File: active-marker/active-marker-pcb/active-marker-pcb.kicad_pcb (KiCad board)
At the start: 2 copper layers, 45 x 35 mm, 47 parts, among them J1 Conn_01x10, J13 Conn_01x04, J2 Conn_01x04, J3 Conn_01x04, J4 Conn_01x04, J5 Conn_01x04, J6 Conn_01x04, J7 Conn_01x04, SW1 SW_DIP_x02, SW2 SW_Push, SW3 SW_Push, SW4 SW_Push, U1 220ADA16, U2 XC6206PxxxMR, U3 VEML6030, U4 VEML6030, U5 MCP2551-I-P, U6 STM32F303K8Tx, Y1 NX3225GA-32M

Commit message: add diode, fix gerber files
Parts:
- added D3: D_Schottky, Diode_SMD:D_SOD-523, B.Cu at (107.2, 99.8)
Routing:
- net +5V: track 88.7 -> 90.9 mm
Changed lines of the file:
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@@
+    )
+  )
+  (footprint "Diode_SMD:D_SOD-523" (layer "B.Cu")
+    (at 107.188 99.786 -90)
+    (descr "http://www.diodes.com/datasheets/ap02001.pdf p.144")
+    (tags "Diode SOD523")
+    (property "Sheetfile" "active-marker-pcb.kicad_sch")
+    (property "Sheetname" "")
+    (attr smd)
+    (fp_text reference "D3" (at 2.322 0 90) (layer "B.SilkS")
+      (effects (font (size 1 1) (thickness 0.15)) (justify mirror))
+    )
+    (fp_text value "D_Schottky" (at 0 -1.4 90) (layer "B.Fab")
+      (effects (font (size 1 1) (thickness 0.15)) (justify mirror))
+    )
+    (fp_text user "${REFERENCE}" (at 0 1.3 90) (layer "B.Fab")
+      (effects (font (size 1 1) (thickness 0.15)) (justify mirror))
+    )
+    (fp_line (start 0.7 -0.6) (end -1.15 -0.6) (layer "B.SilkS") (width 0.12))
+    (fp_line (start -1.15 0.6) (end -1.15 -0.6) (layer "B.SilkS") (width 0.12))
+    (fp_line (start 0.7 0.6) (end -1.15 0.6) (layer "B.SilkS") (width 0.12))
+    (fp_line (start -1.25 -0.7) (end -1.25 0.7) (layer "B.CrtYd") (width 0.05))
+    (fp_line (start -1.25 0.7) (end 1.25 0.7) (layer "B.CrtYd") (width 0.05))
+    (fp_line (start 1.25 -0.7) (end -1.25 -0.7) (layer "B.CrtYd") (width 0.05))
+    (fp_line (start 1.25 0.7) (end 1.25 -0.7) (layer "B.CrtYd") (width 0.05))
+    (fp_line (start -0.2 -0.2) (end -0.2 0.2) (layer "B.Fab") (width 0.1))
+    (fp_line (start 0.1 0) (end 0.25 0) (layer "B.Fab") (width 0.1))
+    (fp_line (start -0.2 0) (end -0.35 0) (layer "B.Fab") (width 0.1))
+    (fp_line (start -0.65 0.45) (end 0.65 0.45) (layer "B.Fab") (width 0.1))
+    (fp_line (start -0.2 0) (end 0.1 -0.2) (layer "B.Fab") (width 0.1))
+    (fp_line (start 0.65 -0.45) (end -0.65 -0.45) (layer "B.Fab") (width 0.1))
+    (fp_line (start 0.65 0.45) (end 0.65 -0.45) (layer "B.Fab") (width 0.1))
+    (fp_line (start 0.1 0.2) (end -0.2 0) (layer "B.Fab") (width 0.1))
+    (fp_line (start -0.65 -0.45) (end -0.65 0.45) (layer "B.Fab") (width 0.1))
+    (fp_line (start 0.1 -0.2) (end 0.1 0.2) (layer "B.Fab") (width 0.1))
+    (pad "1" smd rect (at -0.7 0 90) (size 0.6 0.7) (layers "B.Cu" "B.Paste" "B.Mask")
+      (net 1 "+5V") (pinfunction "K") (pintype "passive"))
+    (pad "2" smd rect (at 0.7 0 90) (size 0.6 0.7) (layers "B.Cu" "B.Paste" "B.Mask")
+      (net 3 "+3V3") (pinfunction "A") (pintype "passive"))
+    (model "${KICAD6_3DMODEL_DIR}/Diode_SMD.3dshapes/D_SOD-523.wrl"
+      (offset (xyz 0 0 0))
+      (scale (xyz 1 1 1))
+      (rotate (xyz 0 0 0))
     )
   )
@@
   (segment (start 118.074 115.606) (end 118.074 114.707) (width 0.3) (layer "B.Cu") (net 1))
   (segment (start 104.4745 106.382) (end 103.0585 104.966) (width 0.5) (layer "B.Cu") (net 1))
+  (segment (start 105.906 98.286) (end 105.345 98.286) (width 0.25) (layer "B.Cu") (net 1))
   (segment (start 135.346 113.574) (end 139.599 113.574) (width 0.3) (layer "B.Cu") (net 1))
   (segment (start 103.3335 102.426) (end 103.3335 104.691) (width 0.5) (layer "B.Cu") (net 1))
@@
   (segment (start 140.716 112.457) (end 140.716 105.8595) (width 0.3) (layer "B.Cu") (net 1))
   (segment (start 124.577 116.332) (end 133.604 116.332) (width 0.3) (layer "B.Cu") (net 1))
+  (segment (start 106.706 99.086) (end 105.906 98.286) (width 0.25) (layer "B.Cu") (net 1))
+  (segment (start 107.188 99.086) (end 106.706 99.086) (width 0.25) (layer "B.Cu") (net 1))
   (segment (start 117.348 116.332) (end 124.577 116.332) (width 0.3) (layer "B.Cu") (net 1))
   (segment (start 103.3335 104.691) (end 103.0585 104.966) (width 0.5) (layer "B.Cu") (net 1))

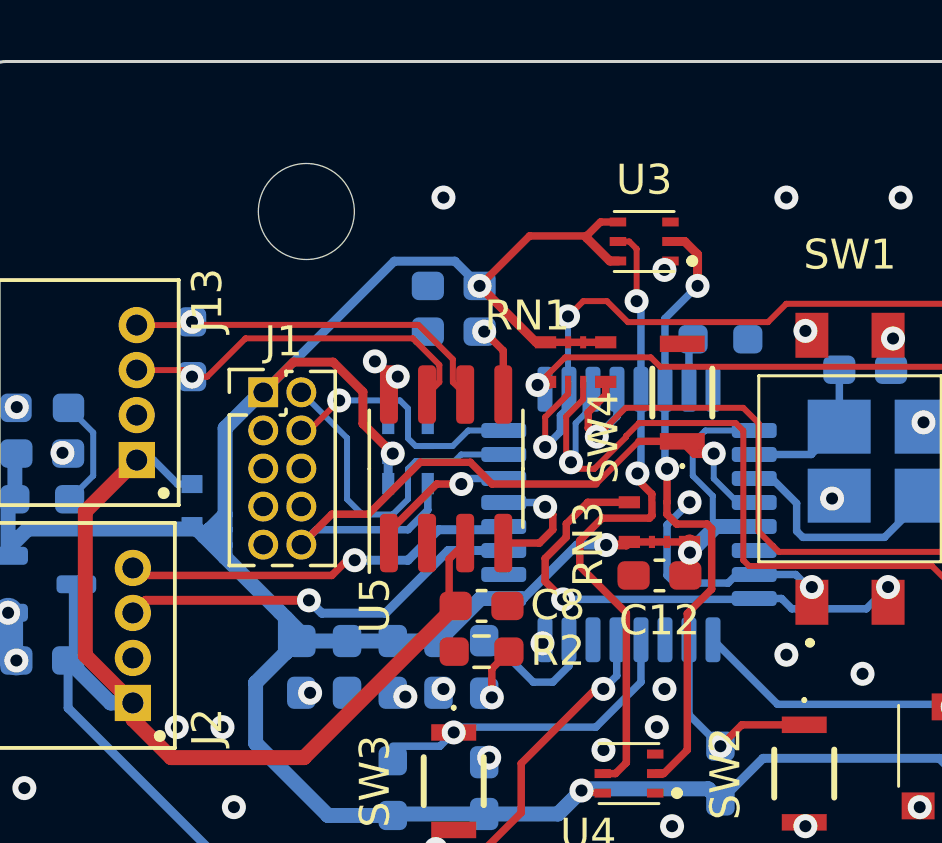
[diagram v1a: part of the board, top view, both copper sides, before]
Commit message: fix a placement of mounting hole
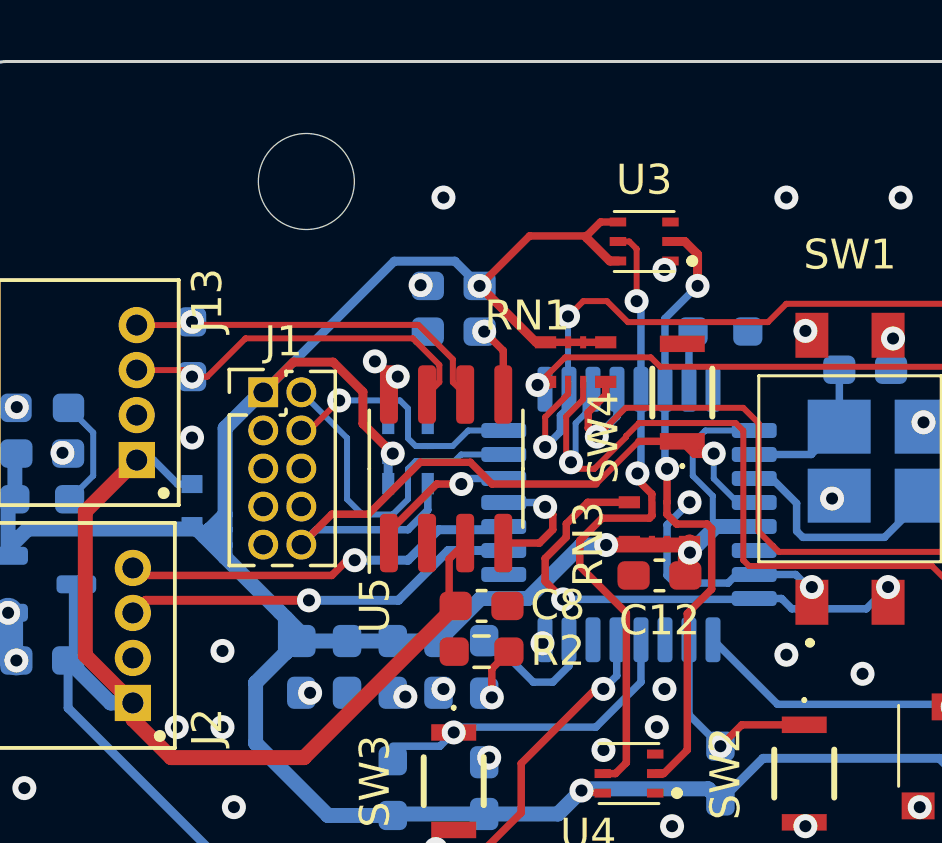
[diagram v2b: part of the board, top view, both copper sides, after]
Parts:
- moved H3 1.00 mm to (111.0, 89.0)
- moved R4 0.26 mm to (124.8, 94.0)
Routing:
- net +3V3: track 109.5 -> 110.3 mm
- net GND: vias 43 -> 46
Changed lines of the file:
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@@
   )
   (footprint "MountingHole:MountingHole_3.2mm_M3_ISO7380" (layer "F.Cu")
-    (at 111 90)
+    (at 111 89)
     (descr "Mounting Hole 3.2mm, no annular, M3, ISO7380")
     (tags "mounting hole 3.2mm no annular m3 iso7380")
@@
   )
   (footprint "Resistor_SMD:R_0603_1608Metric_Pad0.98x0.95mm_HandSolder" (layer "B.Cu")
-    (at 124.802 94.258)
+    (at 124.802 94)
     (descr "Resistor SMD 0603 (1608 Metric), square (rectangular) end terminal, IPC_7351 nominal with elongated pad for handsoldering. (Body size source: IPC-SM-782 page 72, https://www.pcb-3d.com/wordpress/wp-content/uploads/ipc-sm-782a_amendment_1_and_2.pdf), generated with kicad-footprint-generator")
     (tags "resistor handsolder")
@@
   (segment (start 115.8085 104.672) (end 115.8085 104.8225) (width 0.25) (layer "F.Cu") (net 2))
   (via (at 123.19 110.49) (size 0.8) (drill 0.4) (layers "F.Cu" "B.Cu") (free) (net 2))
+  (via (at 107.188 97.536) (size 0.8) (drill 0.4) (layers "F.Cu" "B.Cu") (free) (net 2))
+  (via (at 114.808 92.456) (size 0.8) (drill 0.4) (layers "F.Cu" "B.Cu") (net 2))
   (via (at 131.572 97.028) (size 0.8) (drill 0.4) (layers "F.Cu" "B.Cu") (net 2))
   (via (at 131.445 109.855) (size 0.8) (drill 0.4) (layers "F.Cu" "B.Cu") (net 2))
@@
   (via (at 115.57 89.535) (size 0.8) (drill 0.4) (layers "F.Cu" "B.Cu") (free) (net 2))
   (via (at 120.904 107.95) (size 0.8) (drill 0.4) (layers "F.Cu" "B.Cu") (net 2))
+  (via (at 108.204 104.648) (size 0.8) (drill 0.4) (layers "F.Cu" "B.Cu") (free) (net 2))
   (via (at 118.872 104.394) (size 0.8) (drill 0.4) (layers "F.Cu" "B.Cu") (net 2))
   (via (at 115.57 118.11) (size 0.8) (drill 0.4) (layers "F.Cu" "B.Cu") (free) (net 2))
@@
   (segment (start 123.786 101.37) (end 123.786 101.0271) (width 0.5) (layer "F.Cu") (net 3))
   (segment (start 109.562 96.026) (end 110.568 95.02) (width 0.3) (layer "F.Cu") (net 3))
-  (segment (start 123.6325 101.5235) (end 123.786 101.37) (width 0.3) (layer "F.Cu") (net 3))
+  (segment (start 123.6325 101.5235) (end 123.786 101.37) (width 0.5) (layer "F.Cu") (net 3))
   (segment (start 118.4405 90.814) (end 116.7745 92.48) (width 0.25) (layer "F.Cu") (net 3))
   (segment (start 120.342 90.878) (end 120.342 90.814) (width 0.3) (layer "F.Cu") (net 3))
   (segment (start 120.806 90.35) (end 120.342 90.814) (width 0.25) (layer "F.Cu") (net 3))
+  (segment (start 123.6325 102.132) (end 123.6325 101.5235) (width 0.5) (layer "F.Cu") (net 3))
   (segment (start 120.256379 109.386) (end 120.879 109.386) (width 0.2) (layer "F.Cu") (net 3))
   (segment (start 112.886331 96.01367) (end 112.886331 97.074331) (width 0.3) (layer "F.Cu") (net 3))
   (segment (start 123.786 101.0271) (end 123.7733 101.0144) (width 0.5) (layer "F.Cu") (net 3))
-  (segment (start 123.7733 101.0144) (end 121.7667 101.0144) (width 0.25) (layer "F.Cu") (net 3))
   (segment (start 121.387 90.35) (end 120.806 90.35) (width 0.25) (layer "F.Cu") (net 3))
   (segment (start 116.7745 92.48) (end 118.6541 94.3596) (width 0.3) (layer "F.Cu") (net 3))
-  (segment (start 123.6325 102.132) (end 123.6325 101.5235) (width 0.3) (layer "F.Cu") (net 3))
   (segment (start 121.114 91.65) (end 120.342 90.878) (width 0.3) (layer "F.Cu") (net 3))
   (segment (start 121.387 91.65) (end 121.114 91.65) (width 0.3) (layer "F.Cu") (net 3))
   (segment (start 120.992 101.116) (end 121.6651 101.116) (width 0.3) (layer "F.Cu") (net 3))
+  (segment (start 120.992 101.116) (end 123.532 101.116) (width 0.5) (layer "F.Cu") (net 3))
   (segment (start 118.9727 94.3596) (end 120.6364 94.3596) (width 0.25) (layer "F.Cu") (net 3))
   (segment (start 121.6651 101.116) (end 121.7667 101.0144) (width 0.3) (layer "F.Cu") (net 3))
   (segment (start 112.886331 97.074331) (end 113.88 98.068) (width 0.3) (layer "F.Cu") (net 3))
+  (segment (start 123.532 101.116) (end 123.786 101.37) (width 0.5) (layer "F.Cu") (net 3))
   (segment (start 118.6541 94.3596) (end 118.9727 94.3596) (width 0.3) (layer "F.Cu") (net 3))
   (segment (start 120.170926 109.300547) (end 120.256379 109.386) (width 0.2) (layer "F.Cu") (net 3))
@@
   (segment (start 101.0585 101.476) (end 101.0585 101.2375) (width 0.5) (layer "B.Cu") (net 3))
   (segment (start 124.3975 109.244) (end 124.802 109.6485) (width 0.5) (layer "B.Cu") (net 3))
-  (segment (start 118.233839 102.9) (end 120.017839 101.116) (width 0.3) (layer "B.Cu") (net 3))
   (segment (start 110.9325 104.164) (end 111.086 104.3175) (width 0.5) (layer "B.Cu") (net 3))
   (segment (start 101.712 100.584) (end 107.3525 100.584) (width 0.5) (layer "B.Cu") (net 3))
+  (segment (start 120.168934 101.116) (end 120.992 101.116) (width 0.5) (layer "B.Cu") (net 3))
   (segment (start 107.5965 100.828) (end 108.292 101.5235) (width 0.5) (layer "B.Cu") (net 3))
   (segment (start 120.170926 109.300547) (end 120.227473 109.244) (width 0.5) (layer "B.Cu") (net 3))
@@
   (segment (start 113.93 110.0825) (end 113.88 110.1325) (width 0.5) (layer "B.Cu") (net 3))
   (segment (start 110.12025 103.35175) (end 110.31825 103.54975) (width 0.5) (layer "B.Cu") (net 3))
+  (segment (start 118.233839 102.9) (end 118.384934 102.9) (width 0.5) (layer "B.Cu") (net 3))
   (segment (start 117.579 102.9) (end 116.81 102.9) (width 0.5) (layer "B.Cu") (net 3))
   (segment (start 101.0585 101.2375) (end 101.712 100.584) (width 0.5) (layer "B.Cu") (net 3))
@@
   (segment (start 110.37425 103.60575) (end 111.086 104.3175) (width 0.5) (layer "B.Cu") (net 3))
   (segment (start 125.929 100.5) (end 124.656 100.5) (width 0.5) (layer "B.Cu") (net 3))
-  (segment (start 107.5965 100.828) (end 107.5965 100.7955) (width 0.5) (layer "B.Cu") (net 3))
   (segment (start 101.0585 101.476) (end 101.0585 99.817) (width 0.5) (layer "B.Cu") (net 3))
-  (segment (start 120.017839 101.116) (end 120.992 101.116) (width 0.3) (layer "B.Cu") (net 3))
   (segment (start 110.302375 103.565625) (end 110.31825 103.54975) (width 0.5) (layer "B.Cu") (net 3))
+  (segment (start 118.384934 102.9) (end 120.168934 101.116) (width 0.5) (layer "B.Cu") (net 3))
   (segment (start 111.7205 110.1325) (end 109.308 107.72) (width 0.5) (layer "B.Cu") (net 3))
   (segment (start 125.929 97.3) (end 124.3 97.3) (width 0.2) (layer "B.Cu") (net 3))
@@
   (segment (start 105.217 103.382) (end 105.638028 102.960972) (width 0.3) (layer "F.Cu") (net 14))
   (via (at 111.086 102.960972) (size 0.8) (drill 0.4) (layers "F.Cu" "B.Cu") (net 14))
-  (segment (start 113.638 103.39) (end 111.515028 103.39) (width 0.3) (layer "B.Cu") (net 14))
+  (segment (start 114.067028 102.960972) (end 111.086 102.960972) (width 0.3) (layer "B.Cu") (net 14))
   (segment (start 117.579 101.3) (end 115.728 101.3) (width 0.3) (layer "B.Cu") (net 14))
-  (segment (start 115.728 101.3) (end 113.638 103.39) (width 0.3) (layer "B.Cu") (net 14))
-  (segment (start 111.515028 103.39) (end 111.086 102.960972) (width 0.3) (layer "B.Cu") (net 14))
+  (segment (start 115.728 101.3) (end 114.067028 102.960972) (width 0.3) (layer "B.Cu") (net 14))
   (segment (start 118.162 108.396695) (end 118.162 110.04) (width 0.25) (layer "F.Cu") (net 15))
   (segment (start 120.899701 105.913701) (end 120.644994 105.913701) (width 0.25) (layer "F.Cu") (net 15))

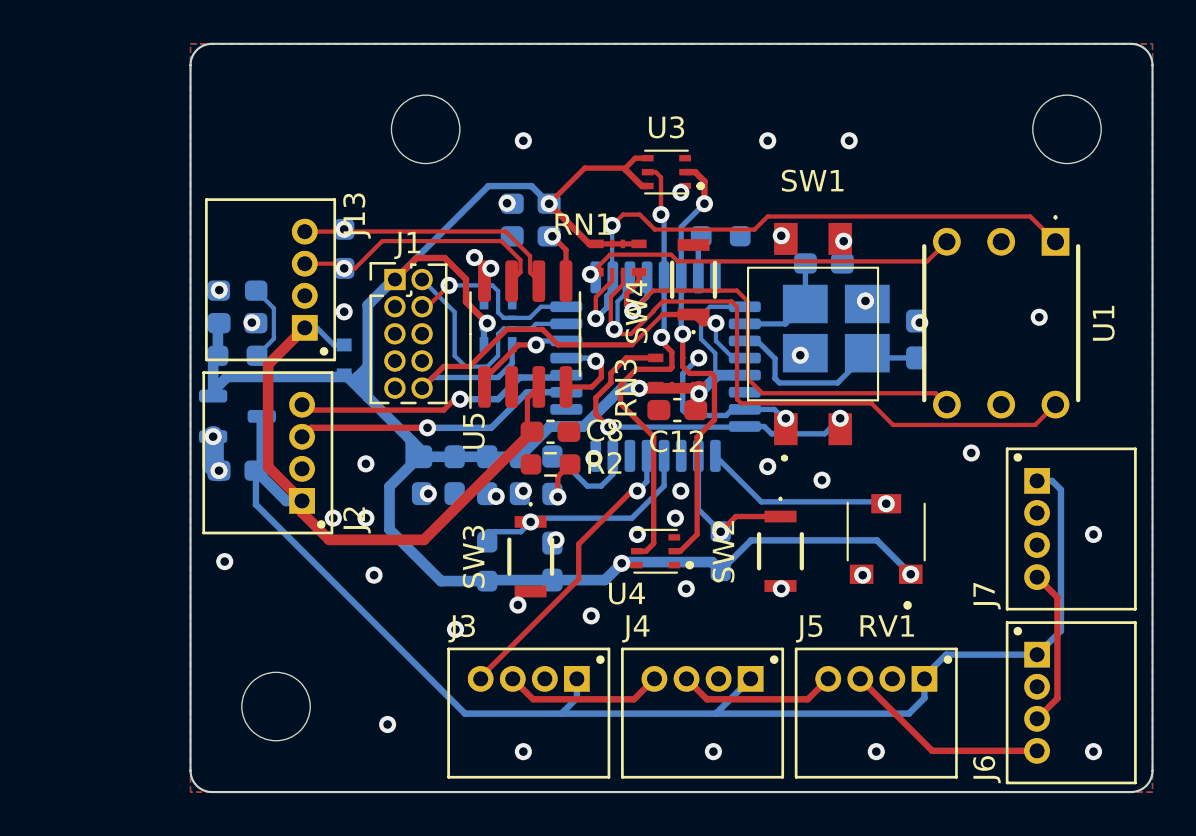
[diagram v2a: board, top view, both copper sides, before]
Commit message: delete can and so on
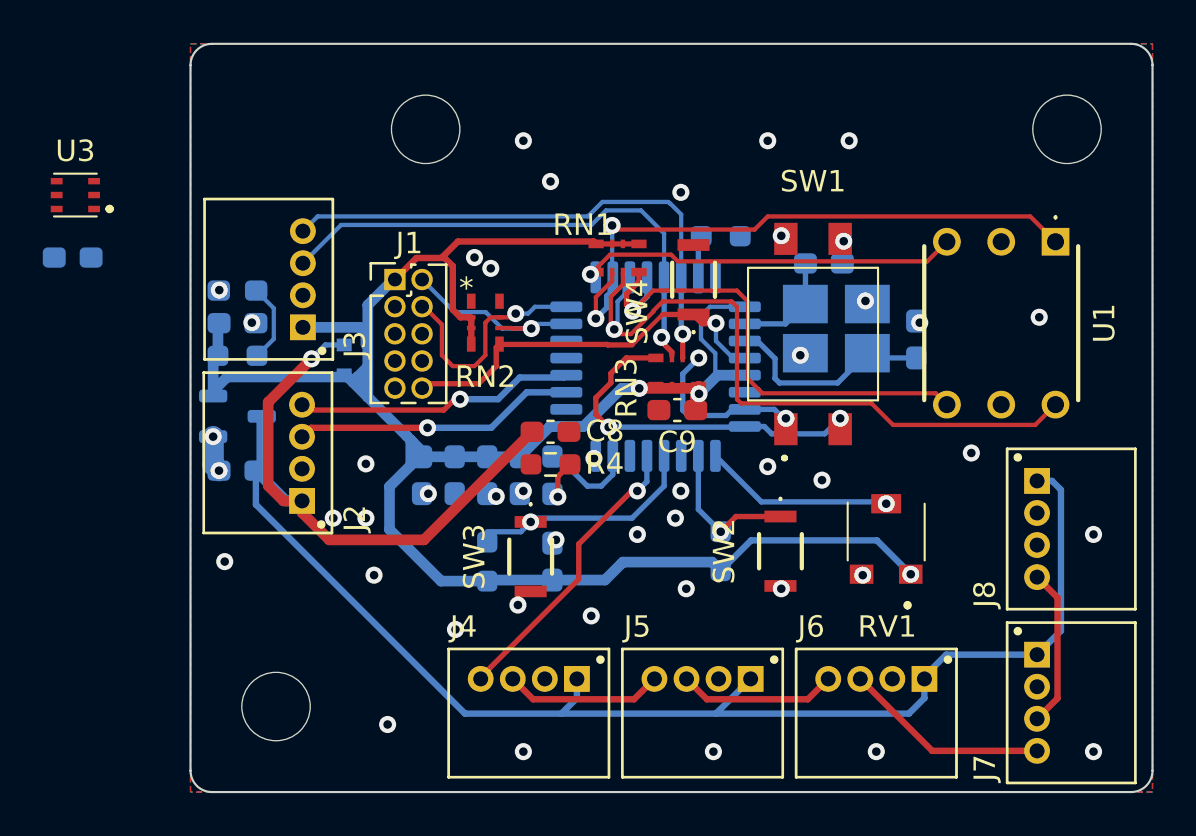
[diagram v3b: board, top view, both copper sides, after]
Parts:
- removed the C5 at (115.9, 94.0)
- removed J13: Conn_01x04, active-marker:JST_S4B-ZR_LF__SN_
- removed the R3 at (107.2, 94.6)
- removed the U4 at (121.8, 108.7)
- removed U5: MCP2551-I-P, Package_SO:SOIC-8_3.9x4.9mm_P1.27mm
- added J3: Conn_01x04, active-marker:JST_S4B-ZR_LF__SN_, F.Cu at (105.3, 96.0)
- RN2: moved to F.Cu
- moved U3 27.7 mm to (94.6, 92.1)
- moved C5 21.6 mm to (94.5, 95.0)
- moved RN2 0.60 mm to (113.8, 98.0)
- renumbered C13 to C10, C6 to C5, C9 to C6, C10 to C7, C11 to C8, C12 to C9, D3 to D1, D1 to D2, D2 to D3, J3 to J4, J4 to J5, J5 to J6, J6 to J7, J7 to J8, R6 to R1, R5 to R2, R1 to R3, R2 to R4, R4 to R5, U6 to U4
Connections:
- RN2 pad 1: +3V3 -> (no net)
- RN2 pad 2: /~{NRST} -> (no net)
- RN2 pad 4: /SWDIO -> /SWCLK
- RN2 pad 6: /SWCLK -> /SWDIO
- RN2 pad 7: (no net) -> +3V3
- RN2 pad 8: (no net) -> /~{NRST}
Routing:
- net /CAN-: track 12.4 -> 0.00 mm, vias 1 -> 0
- net /CAN+: track 12.2 -> 0.00 mm, vias 1 -> 0
- net +3V3: track 110.3 -> 101.2 mm, vias 6 -> 3
- net /~{NRST}: track 24.0 -> 18.4 mm
- net /CAN_TX: track 4.94 -> 0.00 mm, vias 1 -> 0
- net /I2C_SDA: track 21.0 -> 25.3 mm, vias 2 -> 1
- net /CAN_RX: track 4.14 -> 0.00 mm, vias 1 -> 0
- net +5V: track 90.9 -> 87.4 mm, vias 0 -> 1
- net /I2C_SCL: track 21.6 -> 24.3 mm, vias 2 -> 1
- net Net-(C5-Pad1): track 2.36 -> 0.00 mm, vias 1 -> 0
- net /SWCLK: track 8.59 -> 10.8 mm
- net /SWDIO: track 11.1 -> 9.29 mm, vias 0 -> 1
- net GND: vias 46 -> 45
